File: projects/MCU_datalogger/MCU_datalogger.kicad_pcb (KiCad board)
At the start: 2 copper layers, 0 parts

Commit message: MCU datalogger - setup PCBNew
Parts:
- added BT1: Battery, Connector_PinHeader_2.54mm:PinHeader_1x02_P2.54mm_Vertical, F.Cu at (121.1, 104.9)
- added C1: 0.1μF, Capacitor_SMD:C_1206_3216Metric_Pad1.33x1.80mm_HandSolder, F.Cu at (140.0, 95.1)
- added C2: 22pF, Capacitor_SMD:C_1206_3216Metric_Pad1.33x1.80mm_HandSolder, F.Cu at (140.0, 98.4)
- added C3: 22pF, Capacitor_SMD:C_1206_3216Metric_Pad1.33x1.80mm_HandSolder, F.Cu at (140.0, 101.8)
- added C4: 0.1μF, Capacitor_SMD:C_1206_3216Metric_Pad1.33x1.80mm_HandSolder, F.Cu at (140.0, 105.1)
- added C5: 100nF, Capacitor_SMD:C_1206_3216Metric_Pad1.33x1.80mm_HandSolder, F.Cu at (140.0, 108.5)
- added D1: LED, LED_SMD:LED_1206_3216Metric_Pad1.42x1.75mm_HandSolder, F.Cu at (138.2, 86.4)
- added D2: LED, LED_SMD:LED_1206_3216Metric_Pad1.42x1.75mm_HandSolder, F.Cu at (138.2, 89.8)
- added H1: MountingHole, MountingHole:MountingHole_2.2mm_M2, F.Cu at (115.9, 82.5)
- added H2: MountingHole, MountingHole:MountingHole_2.2mm_M2, F.Cu at (115.9, 88.4)
- added H3: MountingHole, MountingHole:MountingHole_2.2mm_M2, F.Cu at (115.9, 94.3)
- added H4: MountingHole, MountingHole:MountingHole_2.2mm_M2, F.Cu at (115.9, 100.3)
- added J1: Conn_01x04_Pin, Connector_PinHeader_2.54mm:PinHeader_1x04_P2.54mm_Vertical, F.Cu at (154.3, 81.8)
- added J2: Conn_01x09_Pin, Connector_PinHeader_2.54mm:PinHeader_1x09_P2.54mm_Vertical, F.Cu at (149.7, 81.8)
- added J3: Conn_01x04_Pin, Connector_PinHeader_2.54mm:PinHeader_1x04_P2.54mm_Vertical, F.Cu at (158.9, 81.8)
- added J4: Conn_02x03_Odd_Even, Connector_PinHeader_2.54mm:PinHeader_2x03_P2.54mm_Vertical, F.Cu at (154.3, 94.0)
- added R1: 10KΩ, Resistor_SMD:R_1206_3216Metric_Pad1.30x1.75mm_HandSolder, F.Cu at (121.8, 81.1)
- added R2: 4.7kΩ, Resistor_SMD:R_1206_3216Metric_Pad1.30x1.75mm_HandSolder, F.Cu at (121.8, 84.4)
- added R3: 10KΩ, Resistor_SMD:R_1206_3216Metric_Pad1.30x1.75mm_HandSolder, F.Cu at (121.8, 87.8)
- added R4: 4.7kΩ, Resistor_SMD:R_1206_3216Metric_Pad1.30x1.75mm_HandSolder, F.Cu at (121.8, 91.1)
- added R5: 330Ω, Resistor_SMD:R_1206_3216Metric_Pad1.30x1.75mm_HandSolder, F.Cu at (121.8, 94.4)
- added R6: 10KΩ, Resistor_SMD:R_1206_3216Metric_Pad1.30x1.75mm_HandSolder, F.Cu at (121.8, 97.7)
- added R7: 330Ω, Resistor_SMD:R_1206_3216Metric_Pad1.30x1.75mm_HandSolder, F.Cu at (121.8, 101.0)
- added U1: 24LC1025, Package_SO:SOIC-8_5.3x5.3mm_P1.27mm, F.Cu at (130.0, 83.0)
- added U2: DS1337S_, MH_DS1337S:SOIC127P600X175-8N, F.Cu at (129.9, 108.0)
- added U3: 24LC1025, Package_SO:SOIC-8_5.3x5.3mm_P1.27mm, F.Cu at (130.0, 90.0)
- added U4: ATMEGA328P-AU, MH_ATMEGA328:QFP80P900X900X120-32N, F.Cu at (131.3, 99.1)
- added Y1: 32.768KHz, Crystal:Crystal_SMD_3215-2Pin_3.2x1.5mm, F.Cu at (115.4, 105.0)
- added Y2: 16MHz, Crystal:Crystal_SMD_5032-2Pin_5.0x3.2mm_HandSoldering, F.Cu at (140.3, 82.1)

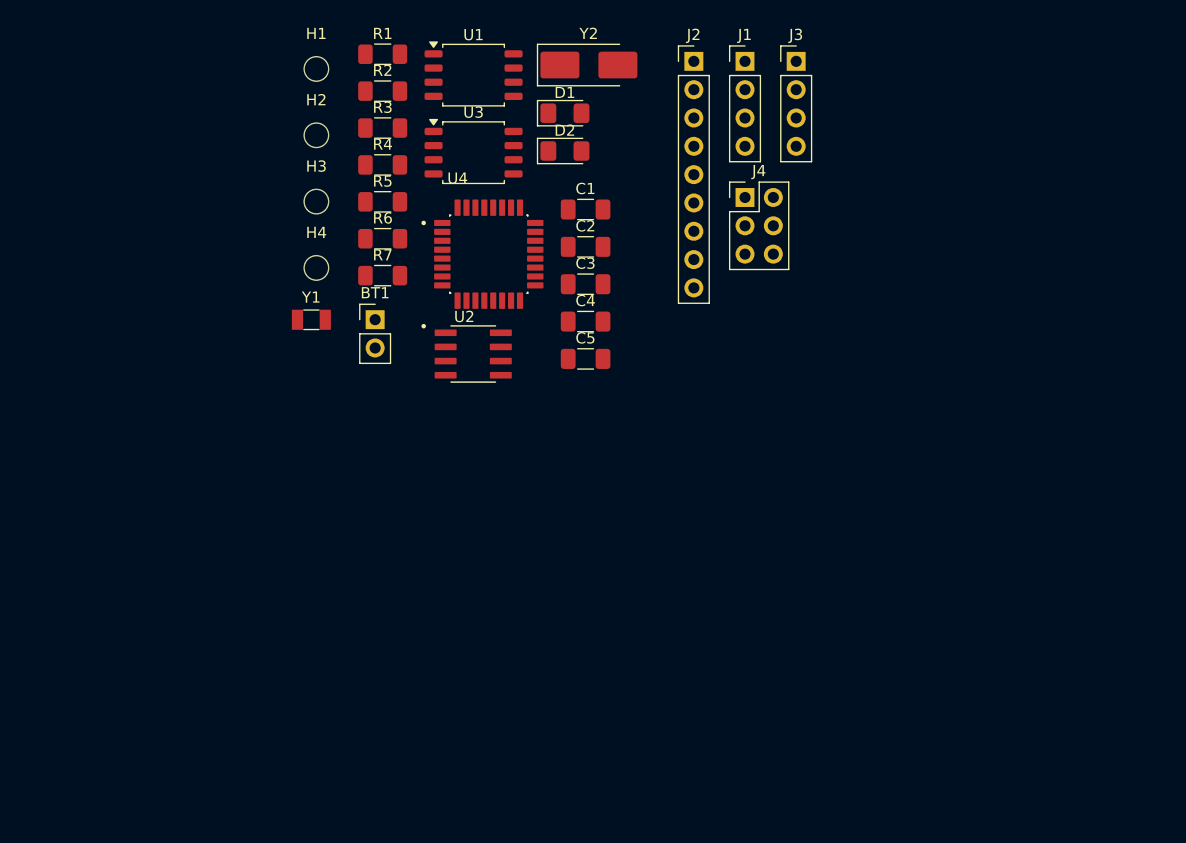
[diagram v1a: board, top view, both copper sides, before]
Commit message: MCU datalogger - initial layout of footprints
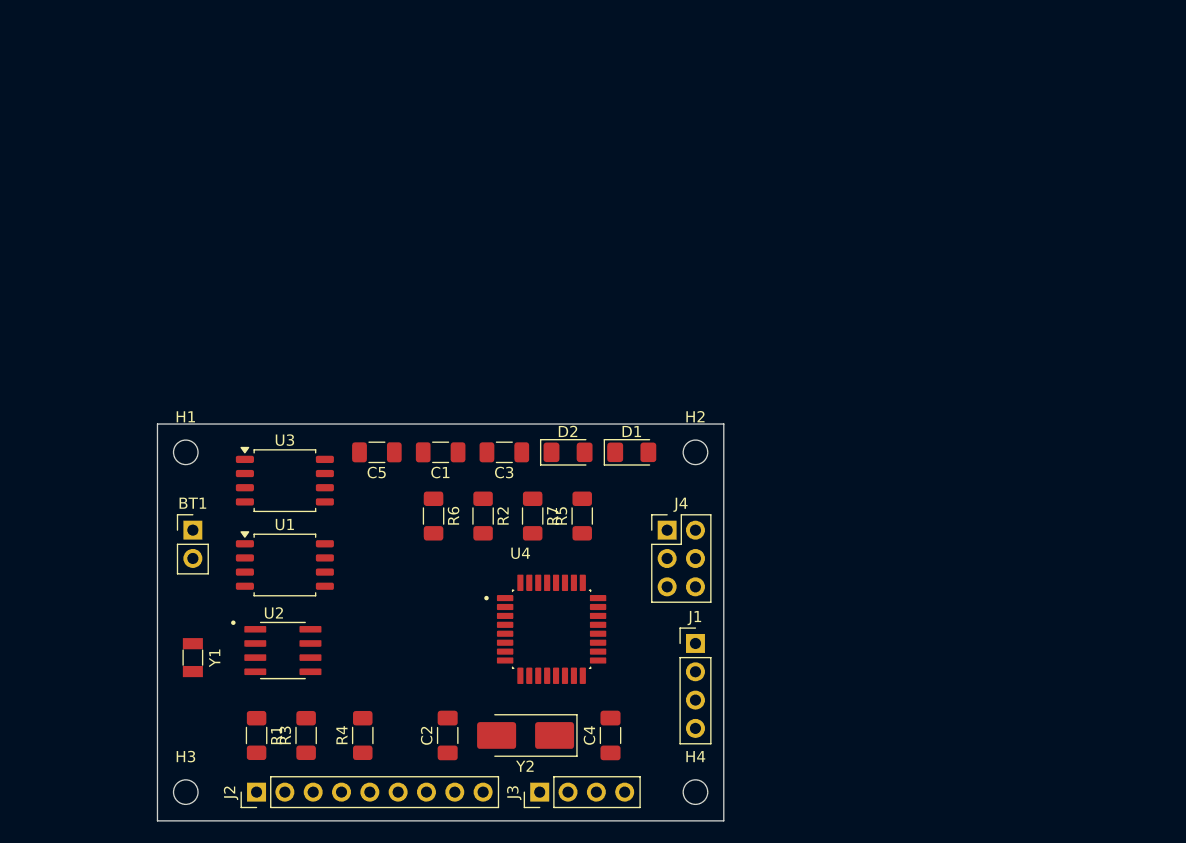
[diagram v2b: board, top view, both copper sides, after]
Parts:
- moved J2 76.4 mm to (110.5, 147.3), turned to 90 degrees
- moved J3 69.5 mm to (135.9, 147.3), turned to 90 degrees
- moved R1 62.1 mm to (110.5, 142.2), turned to -90 degrees
- moved Y2 60.4 mm to (134.6, 142.2), turned to 180 degrees
- moved H4 58.0 mm to (149.9, 147.3)
- moved R3 54.9 mm to (114.9, 142.2), turned to 90 degrees
- moved H3 54.2 mm to (104.1, 147.3)
- moved J1 52.4 mm to (149.9, 134.0)
- moved R4 51.2 mm to (120.0, 142.2), turned to 90 degrees
- moved U1 47.1 mm to (113.0, 126.9)
- moved C2 45.5 mm to (127.6, 142.2), turned to 90 degrees
- moved H2 44.3 mm to (149.9, 116.8)
- moved R2 39.2 mm to (130.8, 122.6), turned to -90 degrees
- moved C4 37.2 mm to (142.2, 142.2), turned to 90 degrees
- moved H1 36.3 mm to (104.1, 116.8)
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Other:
- board outline added: 50.8 x 35.6 mm

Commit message: MCU datalogger - initial routing of the PCB
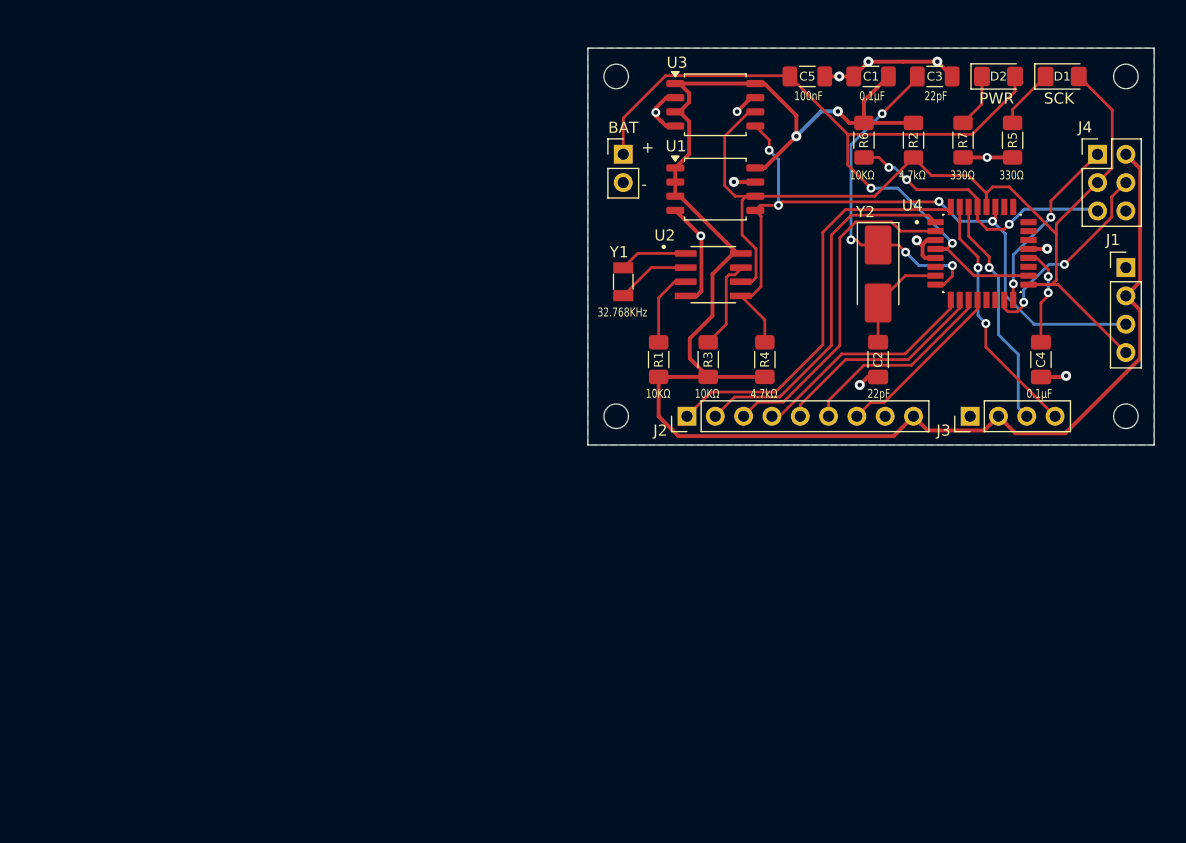
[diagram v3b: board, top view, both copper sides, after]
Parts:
- moved Y2 52.1 mm to (166.2, 100.8), turned to -90 degrees
- moved C4 51.3 mm to (180.8, 108.5)
- moved R6 51.3 mm to (165.0, 88.8)
- moved C1 51.3 mm to (165.6, 83.1)
- moved C3 51.3 mm to (171.3, 83.1)
- moved C5 51.3 mm to (159.9, 83.1)
- moved D2 51.3 mm to (177.0, 83.1)
- moved J2 51.3 mm to (149.1, 113.6)
- moved J4 51.3 mm to (185.9, 90.1)
- moved R2 51.3 mm to (169.4, 88.8)
- moved R5 51.3 mm to (178.3, 88.8)
- moved R7 51.3 mm to (173.9, 88.8)
- moved U1 51.3 mm to (151.6, 93.2)
- moved U2 51.3 mm to (151.5, 100.9)
- moved U3 51.3 mm to (151.6, 85.7)
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- renumbered BT1 to BAT
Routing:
- net /Vcc: track 0.00 -> 152.3 mm, vias 0 -> 2
- net /SCK: track 0.00 -> 91.9 mm
- net Net-(BT1-+): track 0.00 -> 71.2 mm, vias 0 -> 2
- net /SDA: track 0.00 -> 65.0 mm, vias 0 -> 4
- net GND: track 0.00 -> 47.5 mm, vias 0 -> 12
- net /D2: track 0.00 -> 37.4 mm
- net /D3: track 0.00 -> 33.3 mm
- net /D4: track 0.00 -> 30.4 mm
- net Net-(U4-PB7): track 0.00 -> 30.0 mm, vias 0 -> 4
- net /RESET: track 0.00 -> 25.5 mm, vias 0 -> 3
- net /TX: track 0.00 -> 22.3 mm, vias 0 -> 2
- net /RX: track 0.00 -> 20.9 mm, vias 0 -> 1
- net /D5: track 0.00 -> 20.8 mm
- net /D6: track 0.00 -> 19.7 mm
- net /MOSI: track 0.00 -> 18.5 mm, vias 0 -> 2
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- added copper zone on B.Cu, net GND
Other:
- board text added: "+"
- board text added: "-"
- board text added: "PWR"
- board text added: "SCK"

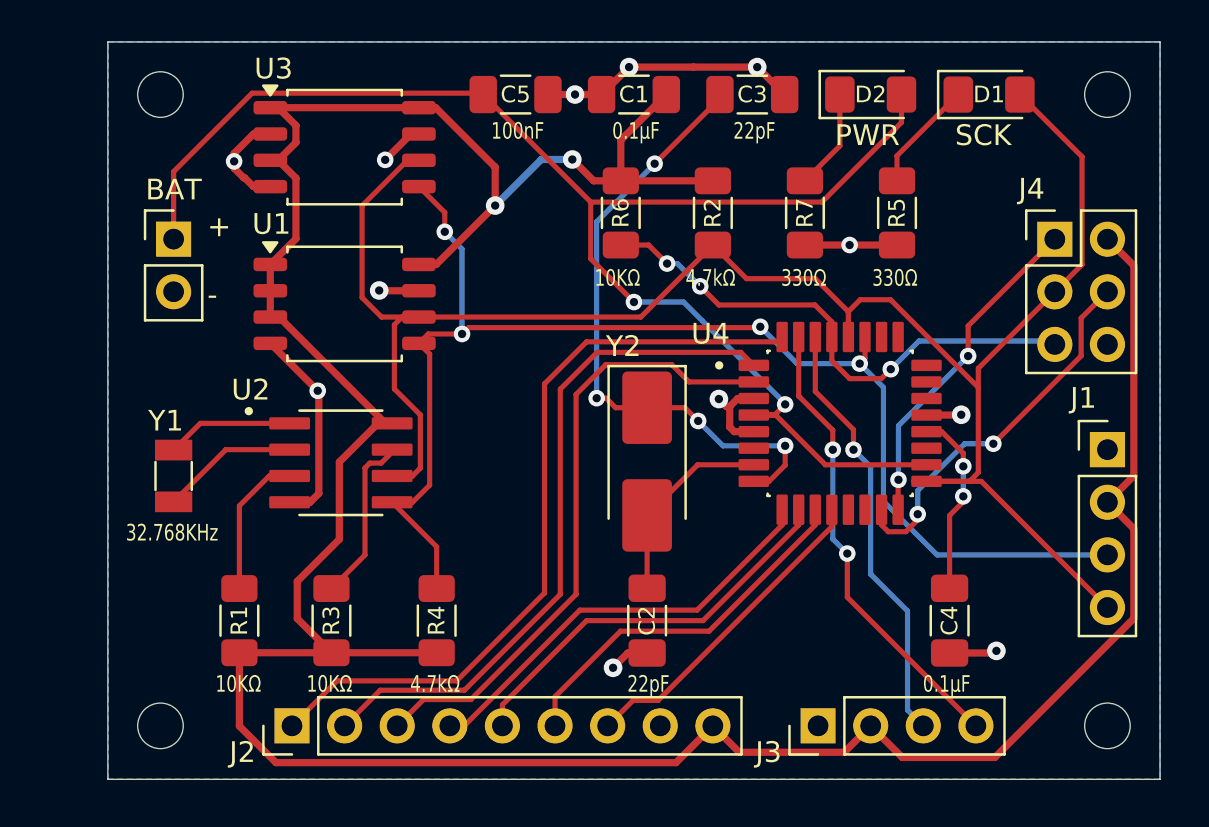
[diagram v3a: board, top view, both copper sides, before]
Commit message: MCU datalogger - v1.0 complete with 3D models and logos
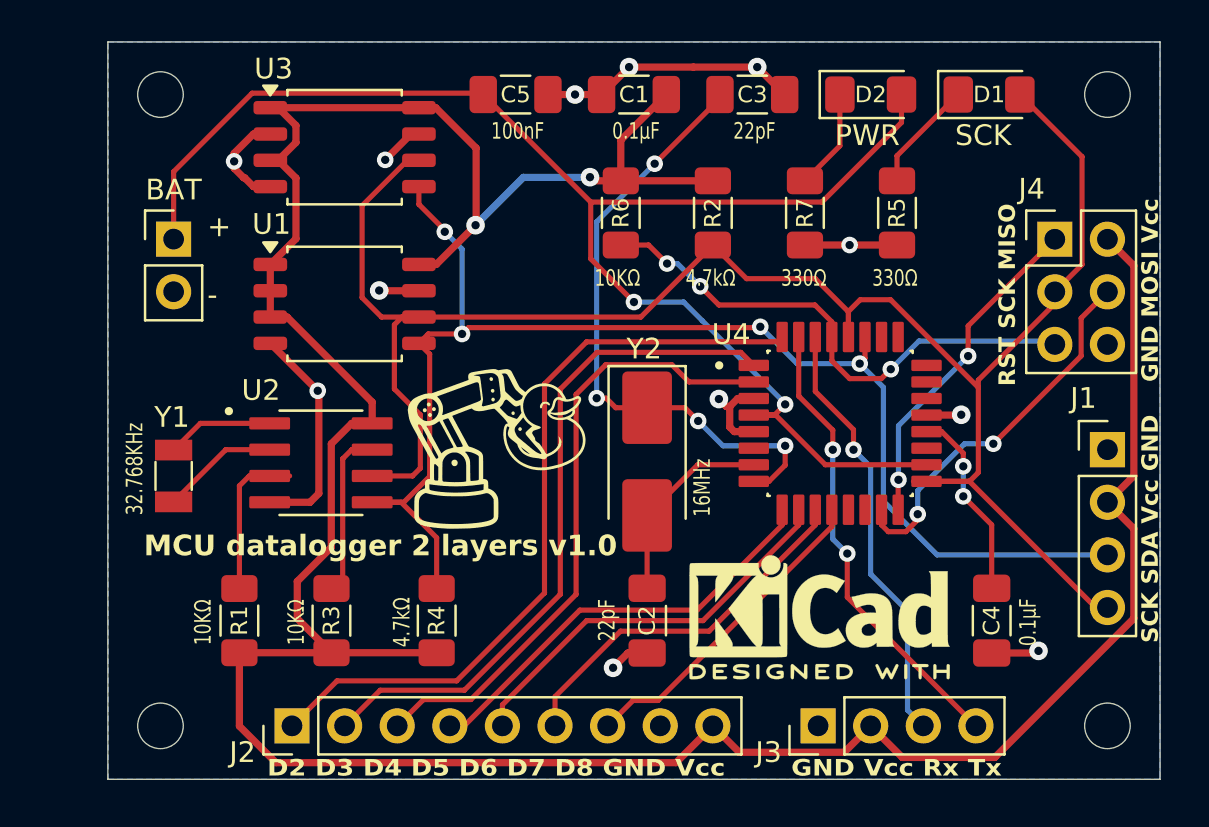
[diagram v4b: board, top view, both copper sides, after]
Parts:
- added G***: LOGO, MH_LOGO:robot_duckie_logo_10mm, F.Cu at (158.9, 99.8)
- added REF**: KiCad-Logo2_5mm_SilkScreen, Symbol:KiCad-Logo2_5mm_SilkScreen, F.Cu at (174.6, 108.3)
- moved C4 2.03 mm to (182.9, 108.5)
- moved U2 0.96 mm to (150.5, 100.9)
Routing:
- net Net-(U2-X2): track 6.64 -> 5.68 mm
- net Net-(U2-X1): track 6.13 -> 5.17 mm
- net /Vcc: track 152.3 -> 151.6 mm
- net Net-(U2-~{INTA}): track 7.02 -> 7.60 mm
- net Net-(U4-AREF): track 9.00 -> 9.56 mm
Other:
- board text added: "D2 D3 D4 D5 D6 D7 D8 GND Vcc"
- board text added: "GND MOSI Vcc"
- board text added: "GND Vcc Rx Tx"
- board text added: "MCU datalogger 2 layers v1.0"
- board text added: "RST SCK MISO"
- board text added: "SCK SDA Vcc GND"

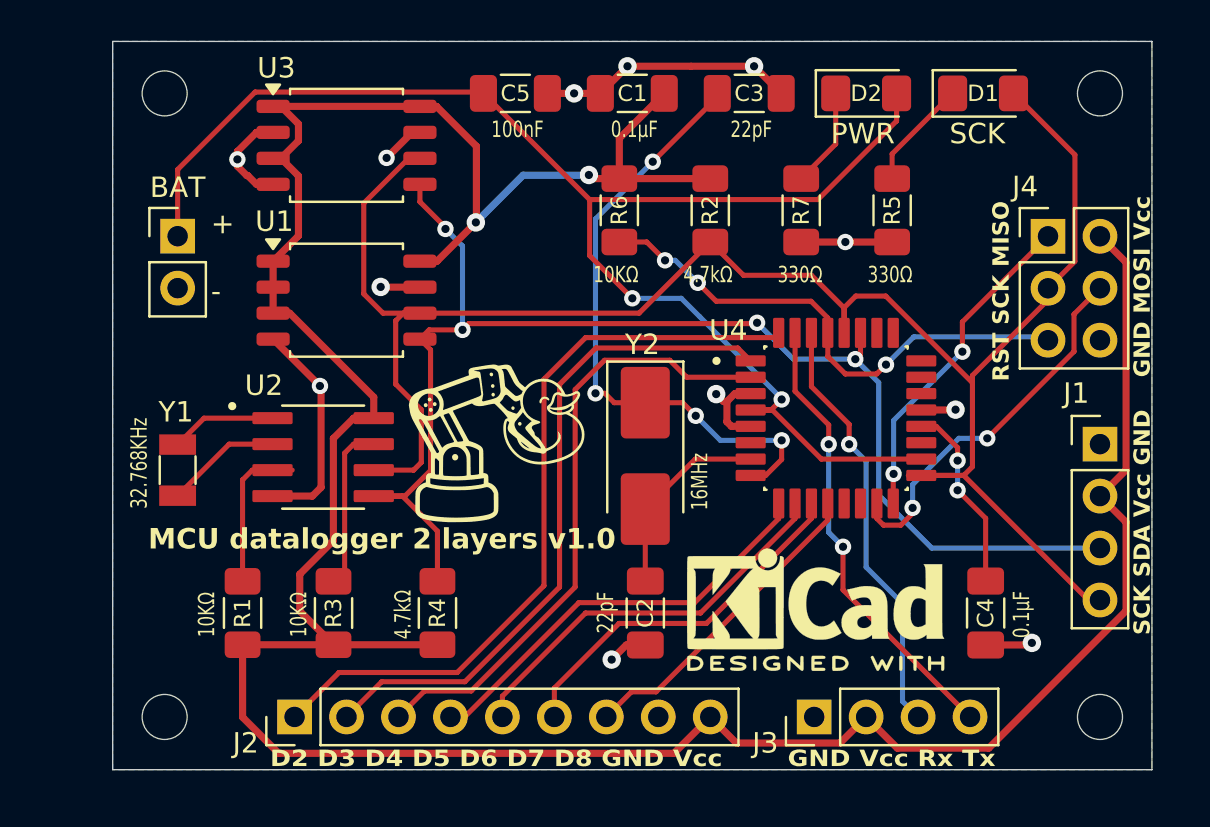
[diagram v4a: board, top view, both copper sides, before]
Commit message: MCU datalogger - v1.1 fine-tune edges and silkscreen
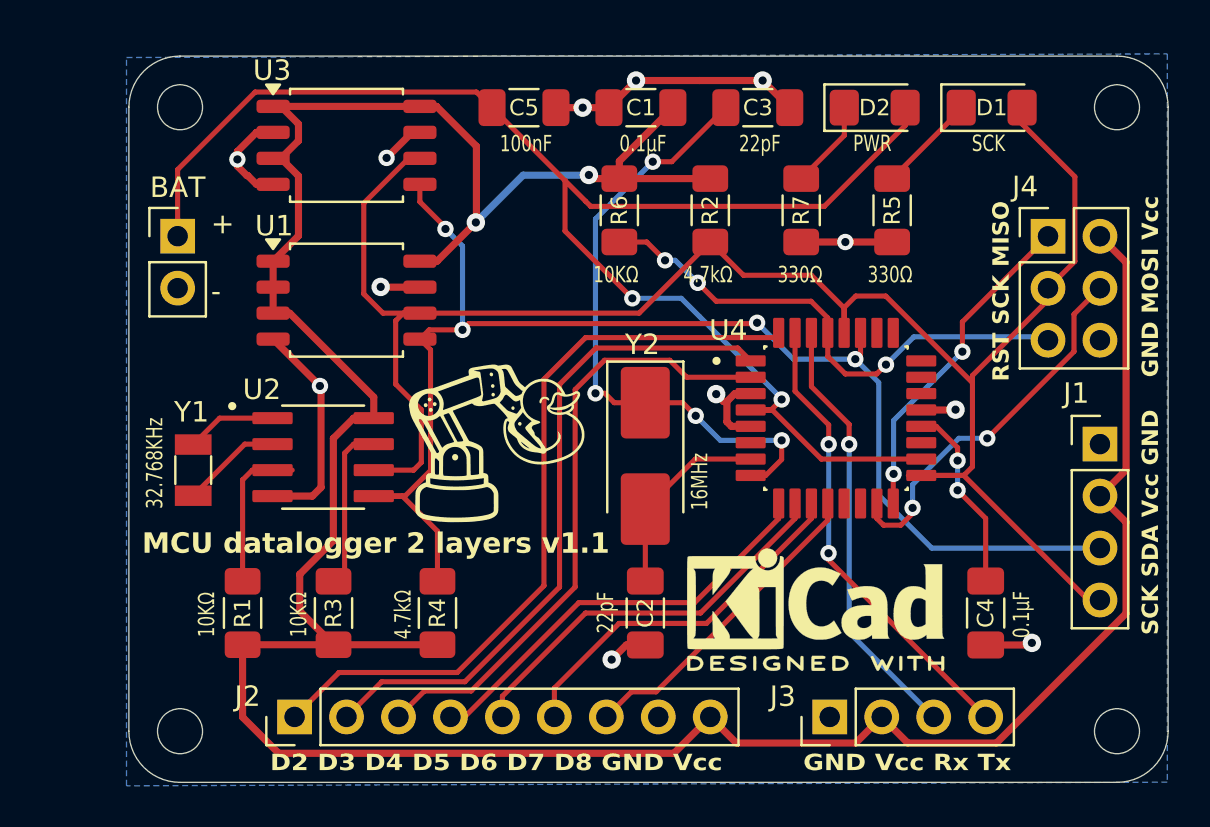
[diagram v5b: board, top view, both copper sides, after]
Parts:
- moved H4 1.09 mm to (189.3, 114.3)
- moved H2 1.07 mm to (189.3, 83.8)
- moved H3 1.03 mm to (143.5, 114.3)
- moved H1 1.01 mm to (143.5, 83.8)
- moved D1 0.81 mm to (183.2, 83.8)
- moved C1 0.81 mm to (166.0, 83.8)
- moved C3 0.81 mm to (171.7, 83.8)
- moved C5 0.81 mm to (160.3, 83.8)
- moved D2 0.81 mm to (177.5, 83.8)
- moved J3 0.76 mm to (175.3, 113.6)
- moved Y1 0.76 mm to (144.1, 101.5)
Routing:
- net Net-(BT1-+): track 71.2 -> 72.8 mm
- net /SCK: track 91.9 -> 91.0 mm
- net Net-(U2-X2): track 5.68 -> 4.92 mm
- net Net-(U2-X1): track 5.17 -> 4.41 mm
- net /Vcc: track 151.6 -> 150.9 mm
- net Net-(D1-K): track 5.39 -> 4.87 mm
- net Net-(D2-K): track 4.86 -> 4.34 mm
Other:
- board size 50.8 x 35.6 mm -> 50.8 x 35.5 mm
- board text added: "MCU datalogger 2 layers v1.1"
- board text removed: "MCU datalogger 2 layers v1.0"
